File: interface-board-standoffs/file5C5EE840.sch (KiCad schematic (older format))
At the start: 10 parts, among them Q1 Q_NMOS_GDS, Q2 Q_NMOS_GDS, Q3 Q_NMOS_GDS, Q4 Q_NMOS_GDS

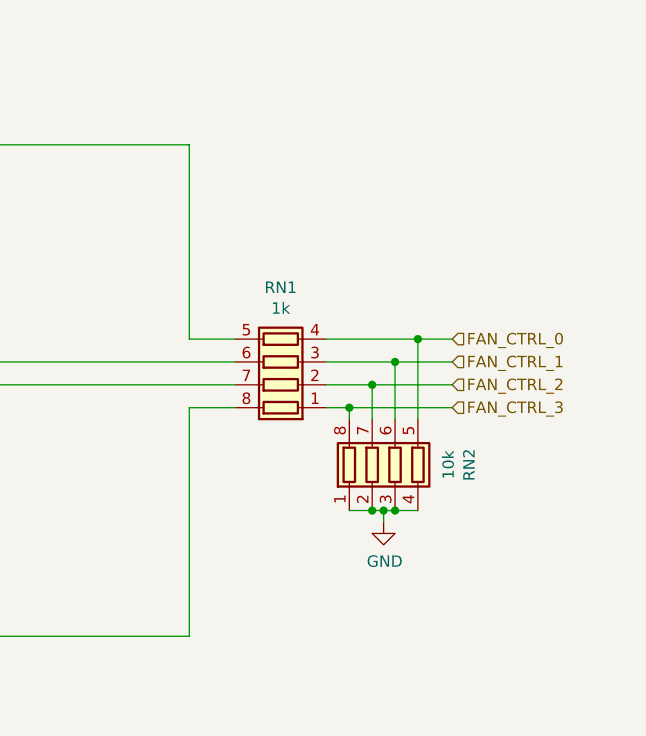
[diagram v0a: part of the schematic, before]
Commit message: Made rev1.1 of interface-board
Added i2c pullups, fixed chip pinout, added isolation slot, removed secondary DC/DC converter
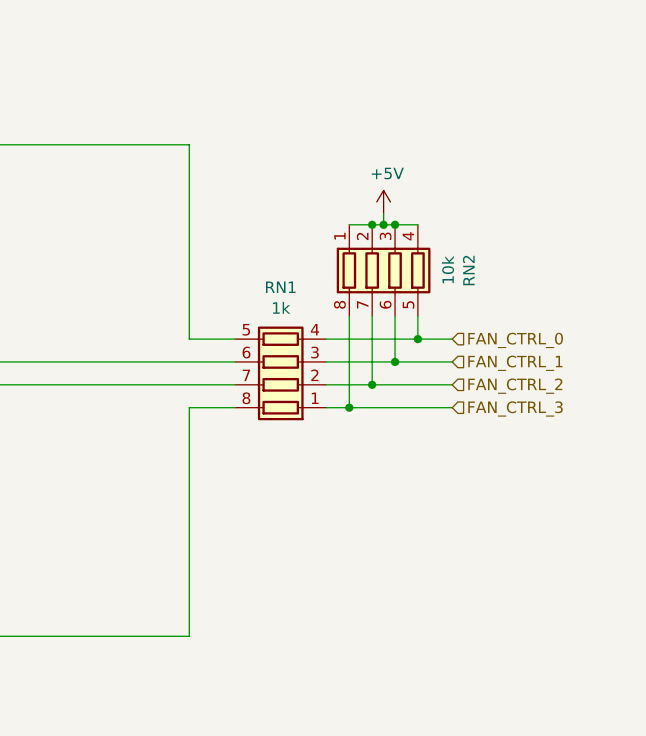
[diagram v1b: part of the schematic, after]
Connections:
- net GND: no longer RN2.1 (R1.1), RN2.2 (R2.1), RN2.3 (R3.1), RN2.4 (R4.1)
- new net +5V: RN2.1 (R1.1), RN2.2 (R2.1), RN2.3 (R3.1), RN2.4 (R4.1)
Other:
- moved on the sheet: RN2
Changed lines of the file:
@@
 	0    -1   -1   0
 $EndComp
-Wire Wire Line
-	8750 3300 8850 3300
-Wire Wire Line
-	8850 3300 8850 3350
-Wire Wire Line
-	8750 3200 8950 3200
-Wire Wire Line
-	8950 3200 8950 3350
-Wire Wire Line
-	8750 3100 9050 3100
-Wire Wire Line
-	9050 3100 9050 3350
-Wire Wire Line
-	8750 3000 9150 3000
-Wire Wire Line
-	9150 3000 9150 3350
-$Comp
-L power:GND #PWR?
-U 1 1 5C62559D
-P 9000 3800
-AR Path="/5C62559D" Ref="#PWR?"  Part="1"
-AR Path="/5C5EE841/5C62559D" Ref="#PWR0101"  Part="1"
-AR Path="/5C83278E/5C8304B2/5C62559D" Ref="#PWR0101"  Part="1"
-F 0 "#PWR0101" H 9000 3550 50  0001 C CNN
-F 1 "GND" H 9005 3627 50  0000 C CNN
-F 2 "" H 9000 3800 50  0001 C CNN
-F 3 "" H 9000 3800 50  0001 C CNN
-	1    9000 3800
-	1    0    0    -1
-$EndComp
-Connection ~ 8850 3300
-Wire Wire Line
-	8950 3200 9300 3200
-Connection ~ 8950 3200
-Wire Wire Line
-	9050 3100 9300 3100
-Connection ~ 9050 3100
-Wire Wire Line
-	9150 3000 9300 3000
-Connection ~ 9150 3000
 $Comp
 L Device:Q_NMOS_GDS Q?
@@
 Wire Wire Line
 	8150 3300 8350 3300
-Wire Wire Line
-	8850 3300 9300 3300
 $Comp
 L Device:R_Pack04 RN2
 U 1 1 5C5E5503
-P 9050 3550
+P 9050 2700
 AR Path="/5C5EE841/5C5E5503" Ref="RN2"  Part="1"
 AR Path="/5C83278E/5C8304B2/5C5E5503" Ref="RN2"  Part="1"
-F 0 "RN2" V 9375 3550 50  0000 C CNN
-F 1 "10k" V 9284 3550 50  0000 C CNN
-F 2 "Resistor_SMD:R_Array_Convex_4x0603" V 9325 3550 50  0001 C CNN
-F 3 "~" H 9050 3550 50  0001 C CNN
-	1    9050 3550
+F 0 "RN2" V 9375 2700 50  0000 C CNN
+F 1 "10k" V 9284 2700 50  0000 C CNN
+F 2 "Resistor_SMD:R_Array_Convex_4x0603" V 9325 2700 50  0001 C CNN
+F 3 "~" H 9050 2700 50  0001 C CNN
+	1    9050 2700
+	1    0    0    1
+$EndComp
+Text Notes 8650 7050 0    100  ~ 0
+Willem Hillier\nUVM AERO\n3/5/2019
+Wire Wire Line
+	8750 3000 9150 3000
+Wire Wire Line
+	8750 3100 9050 3100
+Wire Wire Line
+	8750 3200 8950 3200
+Wire Wire Line
+	8750 3300 8850 3300
+Wire Wire Line
+	8850 2900 8850 3300
+Connection ~ 8850 3300
+Wire Wire Line
+	8850 3300 9300 3300
+Wire Wire Line
+	8950 2900 8950 3200
+Connection ~ 8950 3200
+Wire Wire Line
+	8950 3200 9300 3200
+Wire Wire Line
+	9050 2900 9050 3100
+Connection ~ 9050 3100
+Wire Wire Line
+	9050 3100 9300 3100
+Wire Wire Line
+	9150 2900 9150 3000
+Connection ~ 9150 3000
+Wire Wire Line
+	9150 3000 9300 3000
+$Comp
+L power:+5V #PWR0101
+U 1 1 5CA49D15
+P 9000 2450
+F 0 "#PWR0101" H 9000 2300 50  0001 C CNN
+F 1 "+5V" H 9015 2623 50  0000 C CNN
+F 2 "" H 9000 2450 50  0001 C CNN
+F 3 "" H 9000 2450 50  0001 C CNN
+	1    9000 2450
 	1    0    0    -1
 $EndComp
 Wire Wire Line
-	8850 3750 8950 3750
-Connection ~ 8950 3750
+	8850 2500 8950 2500
+Connection ~ 8950 2500
 Wire Wire Line
-	8950 3750 9000 3750
-Connection ~ 9050 3750
+	8950 2500 9000 2500
+Connection ~ 9050 2500
 Wire Wire Line
-	9050 3750 9150 3750
+	9050 2500 9150 2500
 Wire Wire Line
-	9000 3750 9000 3800
-Connection ~ 9000 3750
+	9000 2450 9000 2500
+Connection ~ 9000 2500
 Wire Wire Line
-	9000 3750 9050 3750
-Text Notes 8650 7050 0    100  ~ 0
-Willem Hillier\nUVM AERO\n3/5/2019
+	9000 2500 9050 2500
 $EndSCHEMATC
